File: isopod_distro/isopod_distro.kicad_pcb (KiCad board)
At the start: 4 copper layers, 65 x 56.5 mm, 57 parts, among them J1 CHG_IN, J10 IN, J11 IN, J12 IN, J13 IN, J14 IN, J15 IN, J16 BATT, J17 OUT, J18 OUT, J19 OUT, J2 OUT, J20 OUT, J21 OUT, J22 OUT, J23 IN, J24 IN, J25 IN, J26 IN, J27 IN, J28 IN, J29 BAL, J3 OUT, J30 Raspberry_Pi_2_3, J4 OUT, J5 OUT, J6 OUT, J7 OUT, J8 TO_DCDC, J9 FROM_DCDC, Q1 IRLR6225TRPBF, Q2 BSS138, Q3 BSS138, U1 MAX17205, U2 UPU-MAX-M8C, U3 adafruit_tdk_icm-20948

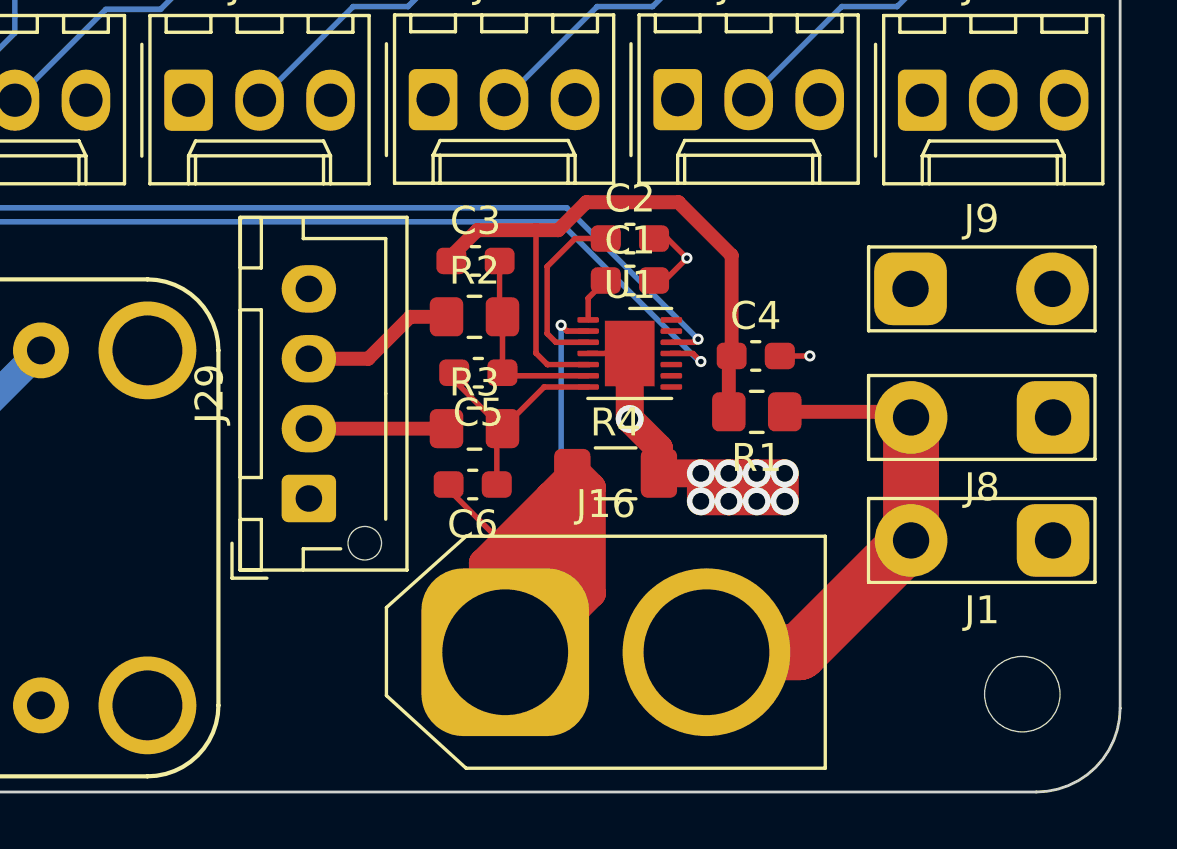
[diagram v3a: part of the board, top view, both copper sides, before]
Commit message: Swap out batt/charge and DC-DC connectors
Use XT30 for battery and charge connectors and MOLEX mini-fit jr 4-way
for the DC-DC converter connection
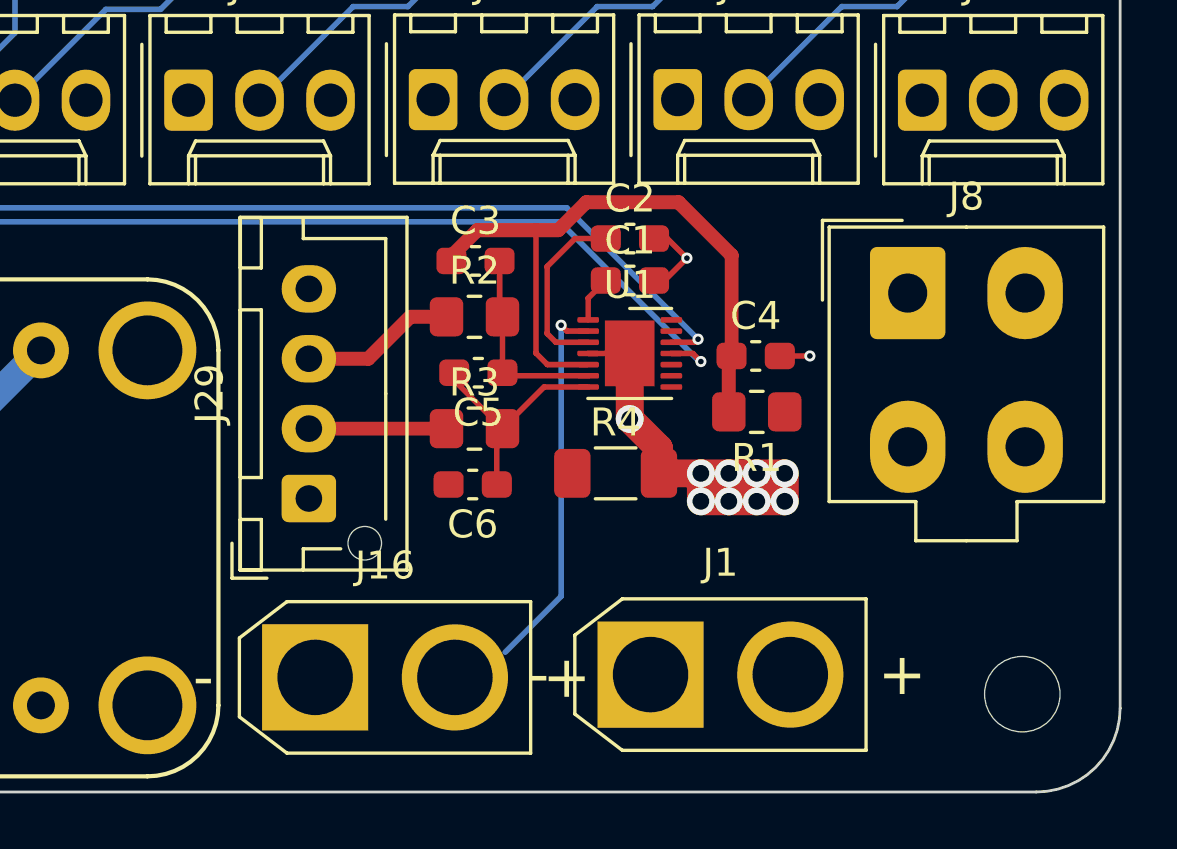
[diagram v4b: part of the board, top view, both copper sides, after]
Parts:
- removed J9: FROM_DCDC, TestPoint:TestPoint_2Pads_Pitch5.08mm_Drill1.3mm
- J1: footprint TestPoint:TestPoint_2Pads_Pitch5.08mm_Drill1.3mm -> Connector_AMASS:AMASS_XT30U-M_1x02_P5.0mm_Vertical
- J16: footprint Connector_AMASS:AMASS_XT60-M_1x02_P7.20mm_Vertical -> Connector_AMASS:AMASS_XT30U-M_1x02_P5.0mm_Vertical
- J8: value TO_DCDC -> DCDC; footprint TestPoint:TestPoint_2Pads_Pitch5.08mm_Drill1.3mm -> Connector_Molex:Molex_Mini-Fit_Jr_5566-04A_2x02_P4.20mm_Vertical
- moved J1 15.2 mm to (198.2, 152.3), turned to 0 degrees
- moved J16 6.86 mm to (186.2, 152.4)
- moved J8 6.84 mm to (207.4, 138.7), turned to 0 degrees
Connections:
- J8 pad 1: GND -> Net-(J1-Pad2)
- J8 pad 2: Net-(J1-Pad2) -> GND
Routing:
- net Net-(C6-Pad2): track 55.4 -> 13.6 mm
- net Net-(J1-Pad2): track 18.0 -> 0.00 mm

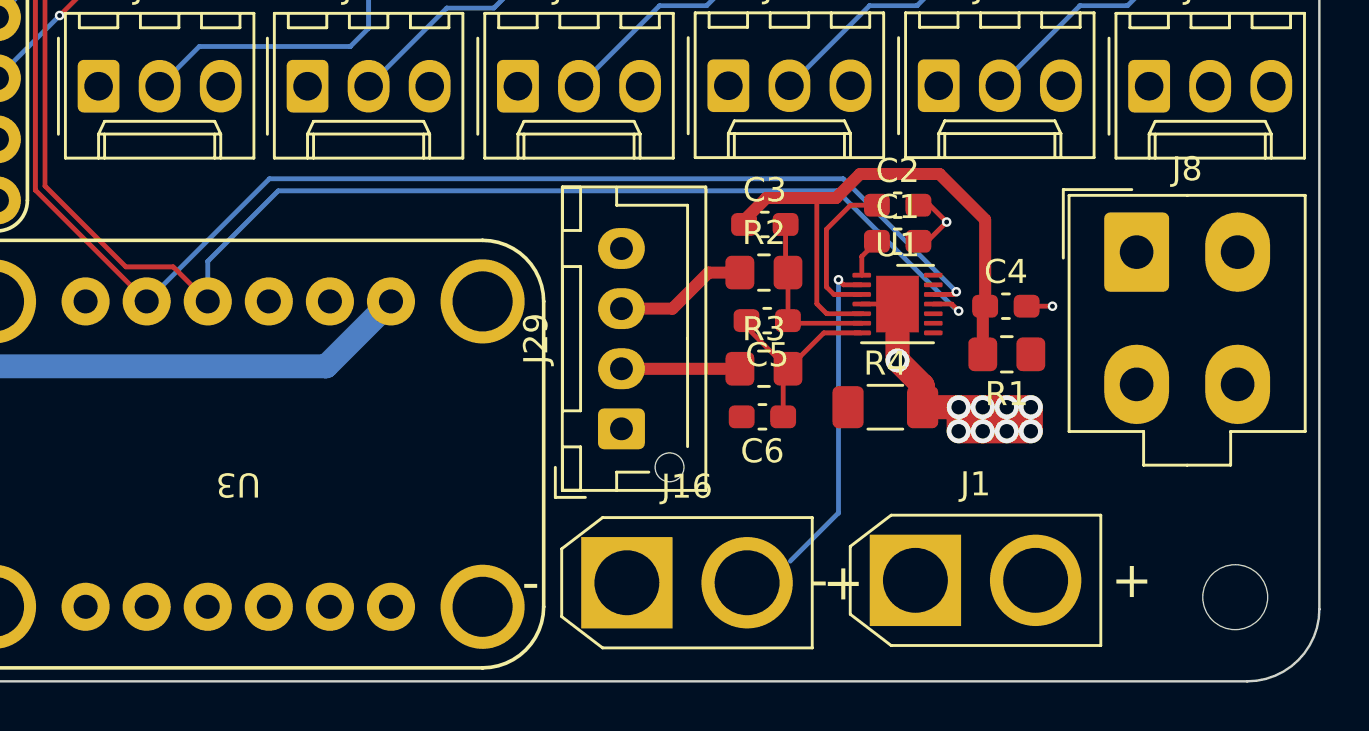
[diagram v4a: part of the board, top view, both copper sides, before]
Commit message: Update PCB with schematic changes
Add the new DNF resistors
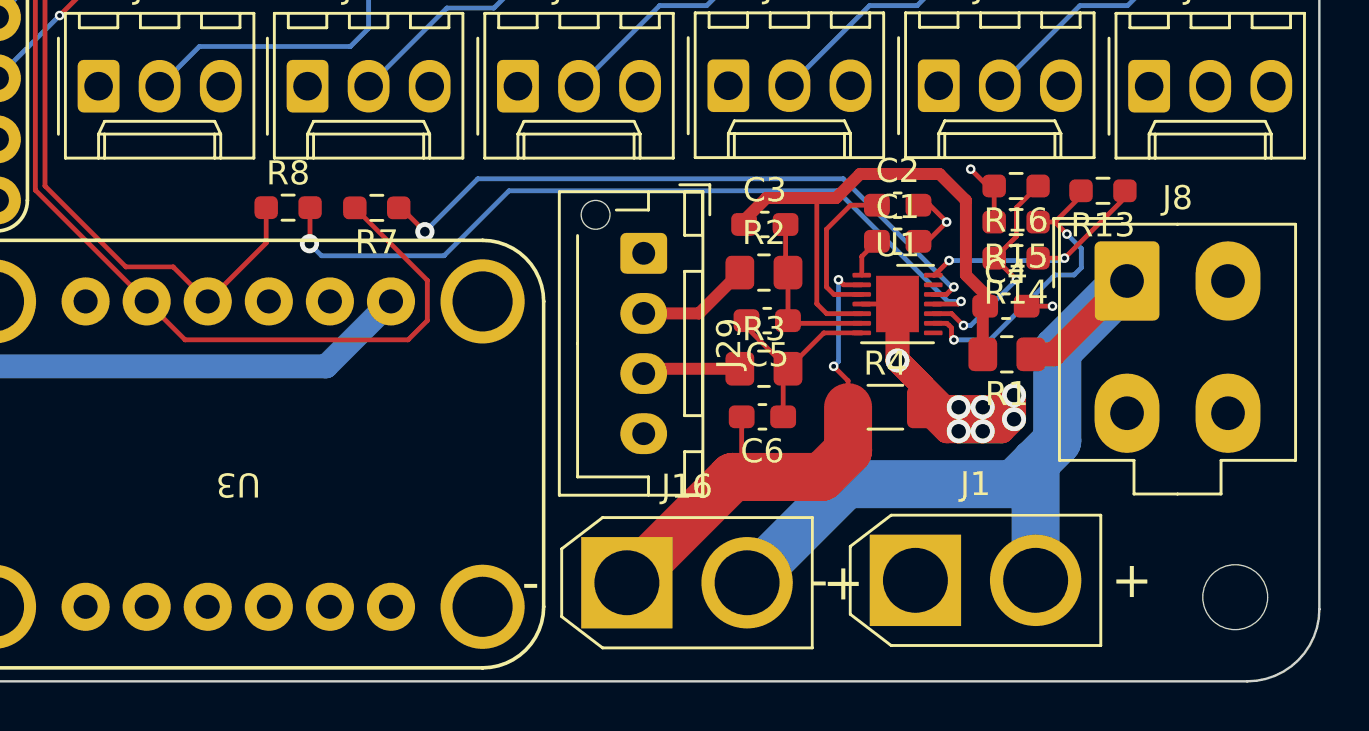
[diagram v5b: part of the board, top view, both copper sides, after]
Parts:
- added R13: DNF, Resistor_SMD:R_0603_1608Metric_Pad0.98x0.95mm_HandSolder, F.Cu at (206.0, 136.1)
- added R14: DNF, Resistor_SMD:R_0603_1608Metric_Pad0.98x0.95mm_HandSolder, F.Cu at (202.4, 138.9)
- added R15: DNF, Resistor_SMD:R_0603_1608Metric_Pad0.98x0.95mm_HandSolder, F.Cu at (202.4, 137.4)
- added R16: DNF, Resistor_SMD:R_0603_1608Metric_Pad0.98x0.95mm_HandSolder, F.Cu at (202.4, 135.9)
- added R7: 150, Resistor_SMD:R_0603_1608Metric_Pad0.98x0.95mm_HandSolder, F.Cu at (175.8, 136.8)
- added R8: 150, Resistor_SMD:R_0603_1608Metric_Pad0.98x0.95mm_HandSolder, F.Cu at (172.1, 136.8)
- moved J29 7.36 mm to (186.9, 138.7), turned to -90 degrees
- moved J8 1.26 mm to (207.0, 139.8)
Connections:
- R2 pad 1: Net-(J29-Pad3) -> Net-(J29-Pad2)
- R3 pad 1: Net-(J29-Pad2) -> Net-(J29-Pad3)
- U1 pad 10: unconnected-(U1-Pad10) -> Net-(R14-Pad2)
- U1 pad 11: /I2C_SCL -> Net-(R8-Pad2)
- U1 pad 12: /I2C_SDA -> Net-(R7-Pad1)
- U1 pad 14: unconnected-(U1-Pad14) -> Net-(R13-Pad1)
- U1 pad 9: unconnected-(U1-Pad9) -> Net-(R13-Pad2)
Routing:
- net Net-(J1-Pad2): track 0.00 -> 33.4 mm
- net Net-(R8-Pad2): track 0.00 -> 33.0 mm, vias 0 -> 2
- net /I2C_SCL: track 89.0 -> 56.5 mm, vias 1 -> 0
- net Net-(R7-Pad1): track 0.00 -> 27.3 mm, vias 0 -> 2
- net GND: track 31.0 -> 51.4 mm, vias 16 -> 15
- net /I2C_SDA: track 89.7 -> 69.6 mm, vias 1 -> 0
- net Net-(R13-Pad2): track 0.00 -> 12.7 mm, vias 0 -> 2
- net Net-(R13-Pad1): track 0.00 -> 10.7 mm, vias 0 -> 2
- net Net-(R14-Pad2): track 0.00 -> 9.49 mm, vias 0 -> 2
- net Net-(C6-Pad2): track 13.6 -> 22.6 mm, vias 1 -> 2
- net +5V: track 3.39 -> 7.44 mm
- net Net-(J29-Pad3): track 5.55 -> 4.08 mm

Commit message: DRC fixes, further refinement
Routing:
- net /LED_GND: track 27.0 -> 62.1 mm, vias 5 -> 9
- net GND: track 51.4 -> 71.5 mm, vias 15 -> 17
- net +5V: track 7.44 -> 9.81 mm
- net Net-(Q1-Pad1): track 6.45 -> 7.34 mm

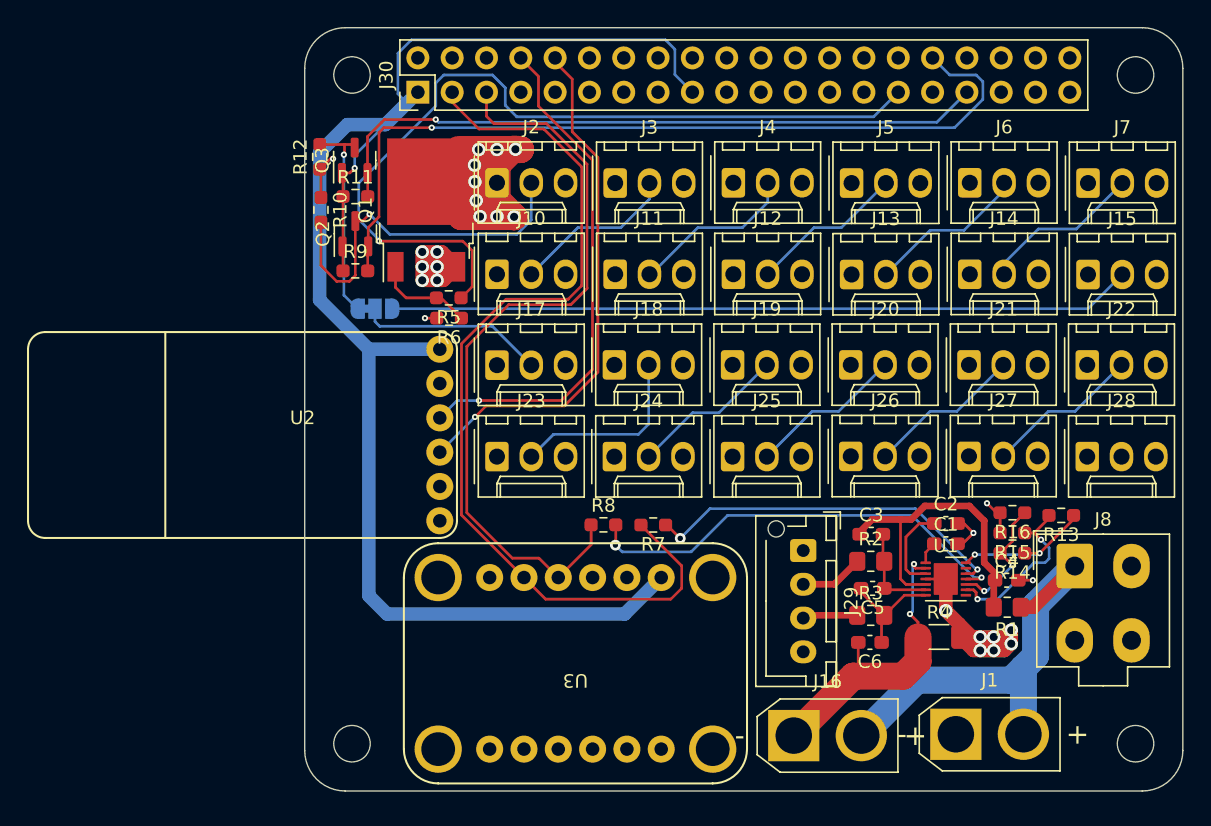
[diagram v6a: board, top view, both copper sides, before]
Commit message: PCB silkscreen
Make the PCB silkscreen look neat: Remove most component references, add
a few values where appropriate, label connectors and pinouts, board name
etc.
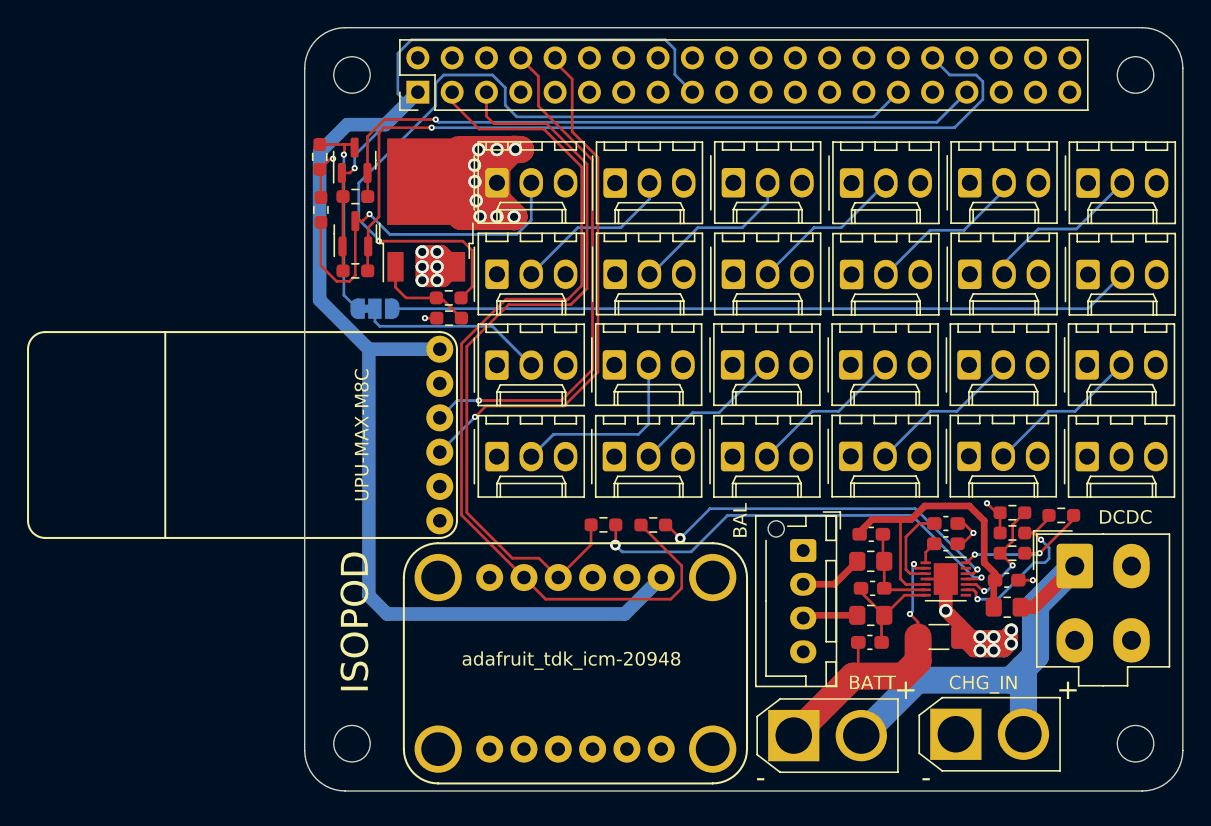
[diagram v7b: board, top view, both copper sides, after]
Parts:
- J10: value IN -> IN 1
- J11: value IN -> IN 2
- J12: value IN -> IN 3
- J13: value IN -> IN 4
- J14: value IN -> IN 5
- J15: value IN -> IN 6
- J17: value OUT -> OUT 7
- J18: value OUT -> OUT 8
- J19: value OUT -> OUT 9
- J2: value OUT -> OUT 1
- J20: value OUT -> OUT 10
- J21: value OUT -> OUT 11
- J22: value OUT -> OUT 12
- J23: value IN -> IN 7
- J24: value IN -> IN 8
- J25: value IN -> IN 9
- J26: value IN -> IN 10
- J27: value IN -> IN 11
- J28: value IN -> IN 12
- J3: value OUT -> OUT 2
- J4: value OUT -> OUT 3
- J5: value OUT -> OUT 4
- J6: value OUT -> OUT 5
- J7: value OUT -> OUT 6
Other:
- board text added: "+"
- board text added: "+5V"
- board text added: "+BATT"
- board text added: "-"
- board text added: "1"
- board text added: "CHAIN"
- board text added: "DATA"
- board text added: "DAVID TURNER MARCH 2022"
- board text added: "GND"
- board text added: "IN 1"
- board text added: "IN 12"
- board text added: "IN 6"
- board text added: "IN 7"
- board text added: "ISOPOD"
- board text added: "OUT 1"
- board text added: "OUT 12"
- board text added: "OUT 6"
- board text added: "OUT 7"
- board text added: "PWM1"
- board text added: "r1"

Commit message: DRC fixes/exclusions
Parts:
- moved R14 0.29 mm to (202.1, 138.9)
- moved R15 0.29 mm to (202.1, 137.4)
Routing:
- net /GPS_RXD: track 38.8 -> 38.0 mm
- net Net-(R13-Pad1): track 10.7 -> 11.4 mm
